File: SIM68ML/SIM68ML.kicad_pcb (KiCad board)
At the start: 2 copper layers, 22.7 x 20.3 mm, 26 parts, among them IC1 SIM68M, J1 Conn_01x05, J2 Conn_01x05, U2 AP7365-W-7

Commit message: GNSS Boards Page Layout Updates
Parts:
- IC1: value SIM68M -> SIM68ML
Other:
- board text added: "SIM68ML www.SirBoard.com"
- board text removed: "SIM68M www.SirBoard.com"
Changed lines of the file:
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@@
   (page User 132.004 102.006)
   (title_block
-    (title "SIM68M Based GPS+GNSS Module")
+    (title "SIM68ML Based GPS+GNSS Module")
     (date 2019-10-31)
     (rev 1)
     (company SirBoard)
-    (comment 1 "SIM68M is based on the MT3333 Chipset")
+    (comment 1 "SIM68ML is based on the MT3333 Chipset")
     (comment 2 "Breadboard Friendly Micro GPS+GNSS Module")
   )
@@
       (effects (font (size 1.27 1.27) (thickness 0.254)))
     )
-    (fp_text value SIM68M (at 4.85 5.05) (layer F.SilkS)
+    (fp_text value SIM68ML (at 4.85 5.05) (layer F.SilkS)
       (effects (font (size 1.27 1.27) (thickness 0.254)))
     )
@@
     )
   )
-  (gr_text "SIM68M\nwww.SirBoard.com" (at 63.4365 31.242 180) (layer B.SilkS)
+  (gr_text "SIM68ML\nwww.SirBoard.com" (at 63.4365 31.242 180) (layer B.SilkS)
     (effects (font (size 1 0.9) (thickness 0.15)) (justify mirror))
   )

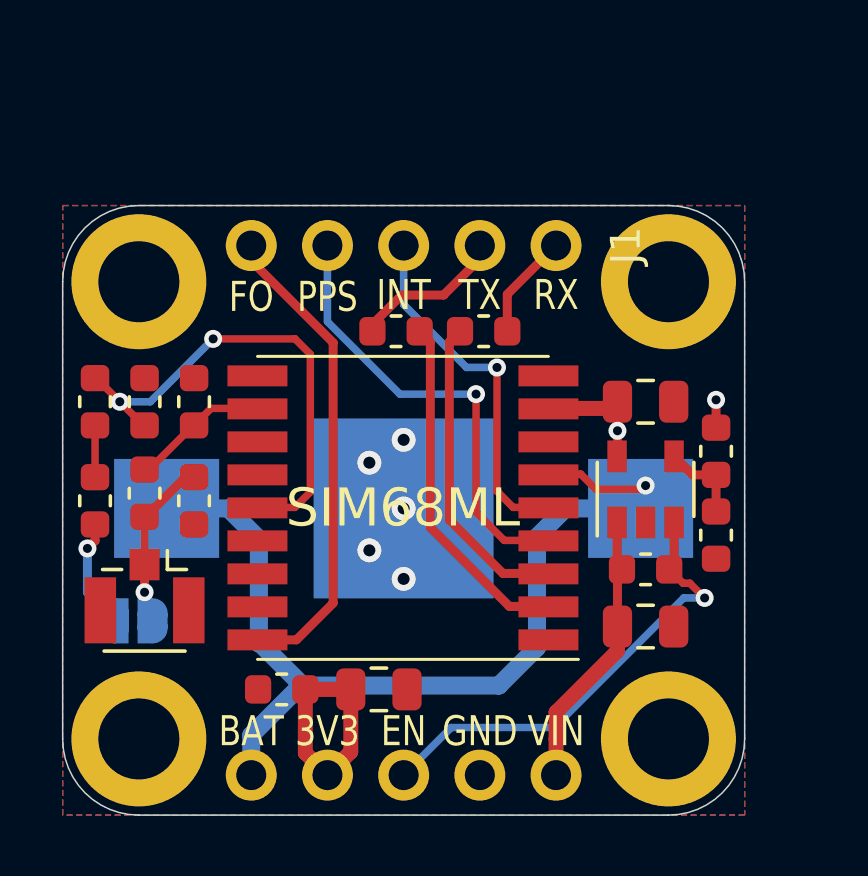
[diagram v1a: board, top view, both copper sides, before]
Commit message: Power LED added
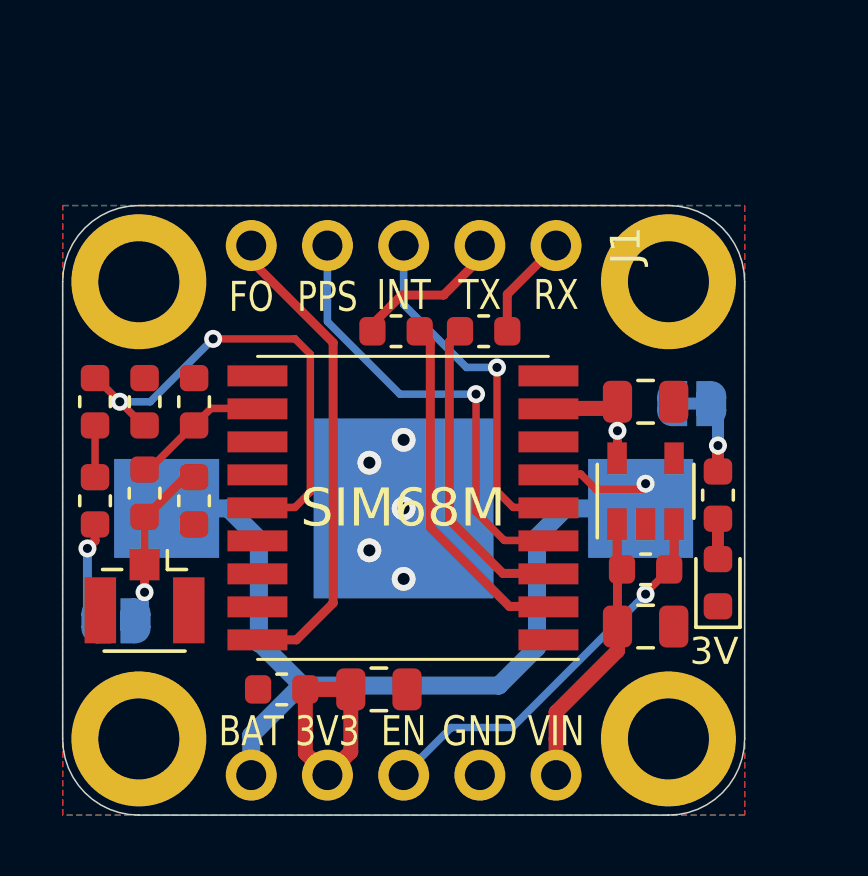
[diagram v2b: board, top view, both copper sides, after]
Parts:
- removed R7: 68K, Resistor_SMD:R_0603_1608Metric
- removed R8: 22K, Resistor_SMD:R_0603_1608Metric
- removed U2: AP7365-W-7, Package_TO_SOT_SMD:SOT-23-5
- added 3V: LED, LED_SMD:LED_0603_1608Metric, F.Cu at (73.9, 39.2)
- added LED: SolderJumper_2_Bridged, Jumper:SolderJumper-2_P1.3mm_Bridged_RoundedPad1.0x1.5mm, B.Cu at (73.0, 33.3)
- added R6: 10R, Resistor_SMD:R_0603_1608Metric, F.Cu at (73.9, 36.3)
- added U1: AP2127K-3.3, Package_TO_SOT_SMD:SOT-23-5, F.Cu at (71.5, 36.2)
- IC1: value SIM68ML -> SIM68M
- moved ANT 0.57 mm to (53.8, 40.5)
- renumbered JP1 to ANT, CR1220 to BT1
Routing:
- net Net-(R7-Pad2): track 2.96 -> 0.00 mm
- net Net-(JP2-Pad2): track 0.00 -> 2.35 mm, vias 0 -> 1
- net EN: track 15.7 -> 13.3 mm
- net Net-(D1-Pad2): track 0.00 -> 1.35 mm
- net 3V3: track 13.0 -> 12.1 mm, vias 2 -> 1

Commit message: Board Sizes Updated
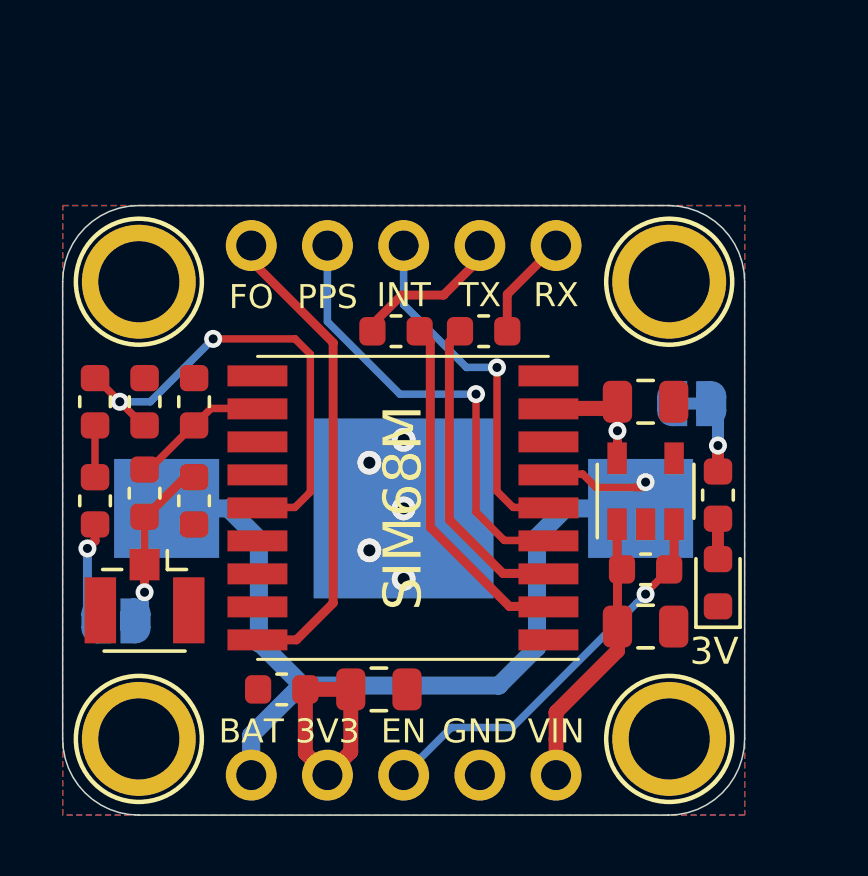
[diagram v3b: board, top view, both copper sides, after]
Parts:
- H1, H2, H3, H4: footprint MountingHole:MountingHole_2.7mm_M2.5_ISO14580_Pad -> SirBoardLibrary:MountingHole_M2.5_SirBoard
- R6: value 10R -> 680E
- moved H4 17.7 mm to (72.3, 29.2), turned to 0 degrees
- moved H3 17.7 mm to (54.6, 44.5), turned to 0 degrees
- moved H2 15.2 mm to (72.3, 44.5), turned to 0 degrees
- moved H1 15.2 mm to (54.6, 29.2), turned to 0 degrees

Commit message: Soldermask width adjusted
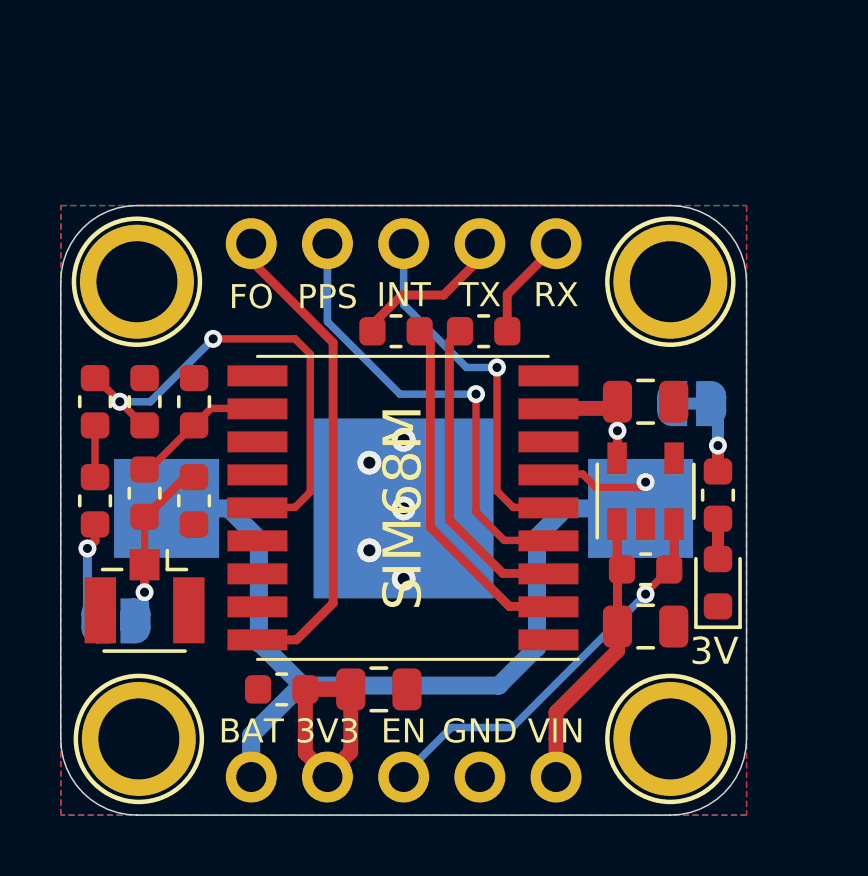
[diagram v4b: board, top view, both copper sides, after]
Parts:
- moved H1 0.06 mm to (54.5, 29.2)
- moved J1 0.06 mm to (68.5, 27.9)
- moved J2 0.06 mm to (68.5, 45.7)
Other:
- board size 22.7 x 20.3 mm -> 22.9 x 20.3 mm
- rule solder_mask_min_width: 0.1 -> 0.05

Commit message: SIM68ML Revision 2
Active Antenna components removed, Battery connector changed
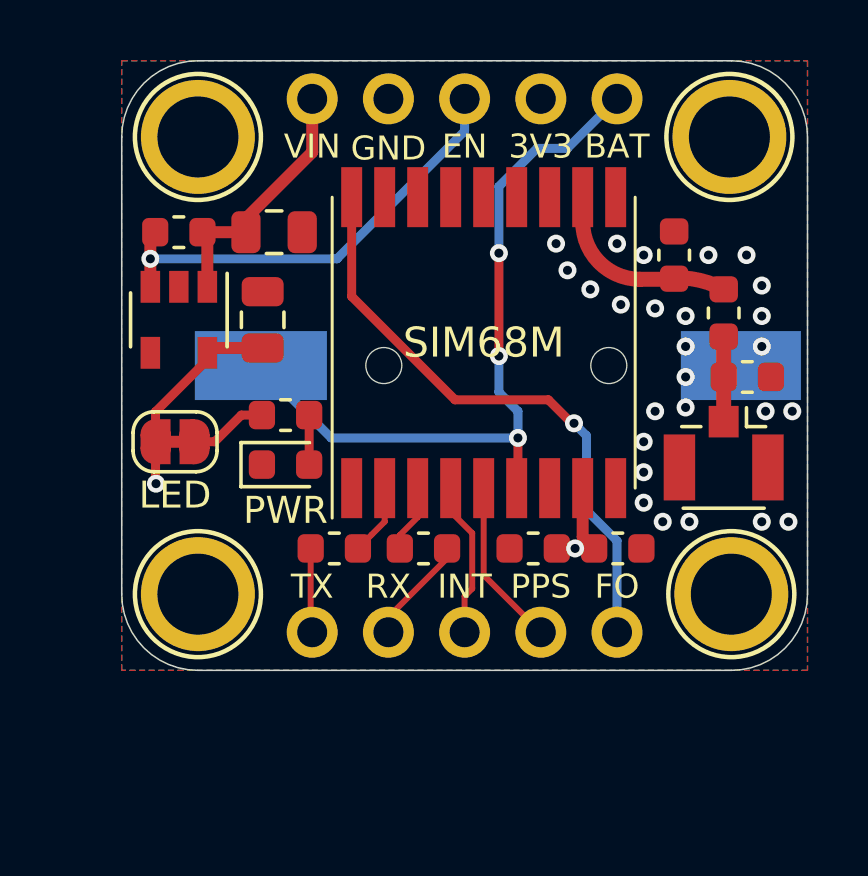
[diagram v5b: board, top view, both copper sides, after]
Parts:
- removed ANT: SolderJumper_2_Open, Jumper:SolderJumper-2_P1.3mm_Open_RoundedPad1.0x1.5mm
- removed C6: 100nF, Capacitor_SMD:C_0603_1608Metric
- removed L1: 27n, Inductor_SMD:L_0603_1608Metric
- removed R5: 10R, Resistor_SMD:R_0603_1608Metric
- added G***: LOGO, logo:SirBoard127x40, B.Cu at (66.5, 32.0)
- added G***: LOGO, logo:OSHW36x26, B.Cu at (56.8, 28.7)
- added G***: LOGO, logo:logo29x41, B.Cu at (57.0, 35.8)
- BT1: footprint Battery:BatteryHolder_Keystone_3000_1x12mm -> SirBoardLibrary:S8411-45R_1
- C1: value 4u7 -> 4.7uF; footprint Capacitor_SMD:C_0805_2012Metric -> Capacitor_SMD:C_0603_1608Metric
- C3, C4: value 1uF -> 10uF
- J1, J2: moved to B.Cu
- LED: moved to F.Cu
- moved H3 28.1 mm to (74.3, 24.4), turned to 180 degrees
- moved H2 25.5 mm to (56.6, 24.4), turned to 180 degrees
- moved J2 24.0 mm to (60.4, 23.1)
- moved H1 22.4 mm to (74.4, 39.6), turned to 180 degrees
- moved R4 20.2 mm to (74.1, 30.3)
- moved AE1 19.9 mm to (74.1, 34.9)
- moved R3 19.2 mm to (55.9, 27.6), turned to 180 degrees
- moved C7 18.9 mm to (74.9, 32.4), turned to 0 degrees
- moved H4 18.9 mm to (56.6, 39.6), turned to 180 degrees
- moved C3 18.1 mm to (59.1, 27.6)
- moved LED 17.3 mm to (55.8, 34.5)
- moved C5 16.7 mm to (72.5, 28.3)
- moved U1 16.6 mm to (55.9, 30.5), turned to 270 degrees
- moved J1 15.3 mm to (60.4, 40.9)
- moved PWR 14.9 mm to (59.5, 35.3), turned to 0 degrees
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- renumbered 3V to PWR
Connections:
- net Net-(C5-Pad1) renamed /ANT
- J1 pad 1: RXD0 -> TXD0
- J1 pad 2: TXD0 -> RXD0
- J1 pad 3: INT -> PPS
- J1 pad 4: PPS -> INT
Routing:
- net Net-(IC1-Pad14): track 16.3 -> 0.00 mm, vias 2 -> 0
- net PPS: track 15.2 -> 5.21 mm, vias 1 -> 0
- net Net-(IC1-Pad2): track 11.7 -> 2.38 mm
- net VBAT: track 33.9 -> 25.1 mm, vias 1 -> 3
- net Net-(IC1-Pad3): track 10.5 -> 2.26 mm
- net INT: track 12.0 -> 5.59 mm, vias 1 -> 0
- net /ANT: track 4.90 -> 0.00 mm
- net F_O: track 16.1 -> 20.0 mm, vias 0 -> 1
- net Net-(JP1-Pad1): track 3.56 -> 0.00 mm, vias 1 -> 0
- net Net-(AE1-Pad1): track 5.80 -> 2.84 mm, vias 1 -> 0
- net TXD0: track 5.16 -> 2.82 mm
- net EN: track 13.3 -> 15.2 mm
- net Net-(L1-Pad2): track 1.73 -> 0.00 mm
- net 3V3: track 12.1 -> 10.4 mm, vias 1 -> 2
- net VIN: track 9.40 -> 8.70 mm
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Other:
- board text added: "CR1220"
- board text added: "LED"
- board text added: "www.SirBoard.com"
- board text removed: "SIM68ML www.SirBoard.com"
